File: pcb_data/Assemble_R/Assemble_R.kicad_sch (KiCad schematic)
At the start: 94 parts, among them J1 Conn_01x02, U1 XIAO-nRF52840

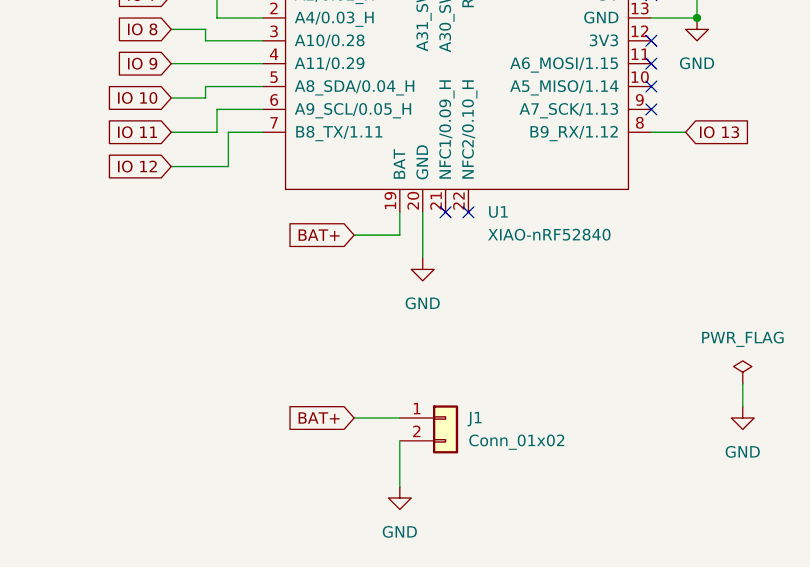
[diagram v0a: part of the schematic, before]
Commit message: add Capacitor symbol
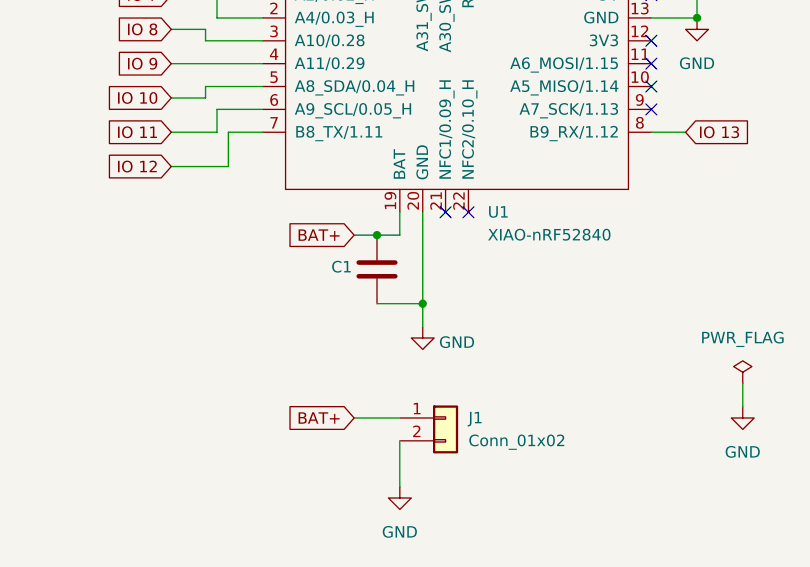
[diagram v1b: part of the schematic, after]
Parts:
- added C1: C, Capacitor_SMD:C_1210_3225Metric_Pad1.33x2.70mm_HandSolder, symbol Device:C
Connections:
- net BAT+: now also C1.1
- net GND: now also C1.2
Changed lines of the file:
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@@
 	)
 	(junction
+		(at 231.14 90.17)
+		(diameter 0)
+		(color 0 0 0 0)
+	)
+	(junction
 		(at 44.45 50.8)
 		(diameter 0)
@@
 	)
 	(junction
+		(at 226.06 82.55)
+		(diameter 0)
+		(color 0 0 0 0)
+	)
+	(junction
 		(at 44.45 91.44)
 		(diameter 0)
@@
 	(wire
 		(pts
+			(xy 226.06 82.55) (xy 228.6 82.55)
+		)
+		(stroke
+			(width 0)
+			(type default)
+		)
+	)
+	(wire
+		(pts
 			(xy 74.93 43.18) (xy 74.93 63.5)
 		)
@@
 	(wire
 		(pts
-			(xy 223.52 82.55) (xy 228.6 82.55)
+			(xy 223.52 82.55) (xy 226.06 82.55)
 		)
 		(stroke
@@
 	(wire
 		(pts
+			(xy 226.06 90.17) (xy 231.14 90.17)
+		)
+		(stroke
+			(width 0)
+			(type default)
+		)
+	)
+	(wire
+		(pts
 			(xy 115.57 27.94) (xy 115.57 43.18)
 		)
@@
 	(wire
 		(pts
+			(xy 231.14 90.17) (xy 231.14 92.71)
+		)
+		(stroke
+			(width 0)
+			(type default)
+		)
+	)
+	(wire
+		(pts
 			(xy 34.29 104.14) (xy 34.29 124.46)
 		)
@@
 	(wire
 		(pts
-			(xy 231.14 80.01) (xy 231.14 85.09)
+			(xy 231.14 80.01) (xy 231.14 90.17)
 		)
 		(stroke
@@
 		(lib_name "GND_2")
 		(lib_id "power:GND")
-		(at 231.14 85.09 0)
+		(at 231.14 92.71 0)
 		(unit 1)
 		(exclude_from_sim no)
@@
 		(on_board yes)
 		(dnp no)
-		(fields_autoplaced yes)
 		(property "Reference" "#PWR02"
-			(at 231.14 91.44 0)
+			(at 231.14 99.06 0)
 			(effects
 				(font
@@
 		)
 		(property "Value" "GND"
-			(at 231.14 90.17 0)
+			(at 234.95 94.488 0)
 			(effects
 				(font
@@
 		)
 		(property "Footprint" ""
-			(at 231.14 85.09 0)
+			(at 231.14 92.71 0)
 			(effects
 				(font
@@
 		)
 		(property "Datasheet" ""
-			(at 231.14 85.09 0)
+			(at 231.14 92.71 0)
 			(effects
 				(font
@@
 		)
 		(property "Description" "Power symbol creates a global label with name \"GND\" , ground"
-			(at 231.14 85.09 0)
+			(at 231.14 92.71 0)
 			(effects
 				(font
@@
 					(unit 1)
 				)
+			)
+		)
+	)
+	(symbol
+		(lib_id "Device:C")
+		(at 226.06 86.36 0)
+		(unit 1)
+		(exclude_from_sim no)
+		(in_bom yes)
+		(on_board yes)
+		(dnp no)
+		(property "Reference" "C1"
+			(at 220.98 86.106 0)
+			(effects
+				(font
+					(size 1.27 1.27)
+				)
+				(justify left)
+			)
+		)
+		(property "Value" "C"
+			(at 221.488 88.9 0)
+			(effects
+				(font
+					(size 1.27 1.27)
+				)
+				(justify left)
+				(hide yes)
+			)
+		)
+		(property "Footprint" "Capacitor_SMD:C_1210_3225Metric_Pad1.33x2.70mm_HandSolder"
+			(at 227.0252 90.17 0)
+			(effects
+				(font
+					(size 1.27 1.27)
+				)
+				(hide yes)
+			)
+		)
+		(property "Datasheet" "~"
+			(at 226.06 86.36 0)
+			(effects
+				(font
+					(size 1.27 1.27)
+				)
+				(hide yes)
+			)
+		)
+		(property "Description" "Unpolarized capacitor"
+			(at 226.06 86.36 0)
+			(effects
+				(font
+					(size 1.27 1.27)
+				)
+				(hide yes)
+			)
+		)
+		(pin "1"
+		)
+		(pin "2"
+		)
+		(instances
+			(project "Assemble_R"
+				(path "/38d74f02-042c-4f1b-a14f-ae40b0d0e57e"
+					(reference "C1")
+					(unit 1)
+				)

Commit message: add model number of capacitor
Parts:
- C1: value C -> GRM32EC81C476KE15L
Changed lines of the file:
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@@
 			)
 		)
-		(property "Value" "C"
+		(property "Value" "GRM32EC81C476KE15L"
 			(at 221.488 88.9 0)
 			(effects
